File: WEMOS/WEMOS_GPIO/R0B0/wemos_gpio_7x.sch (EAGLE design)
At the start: 24 parts

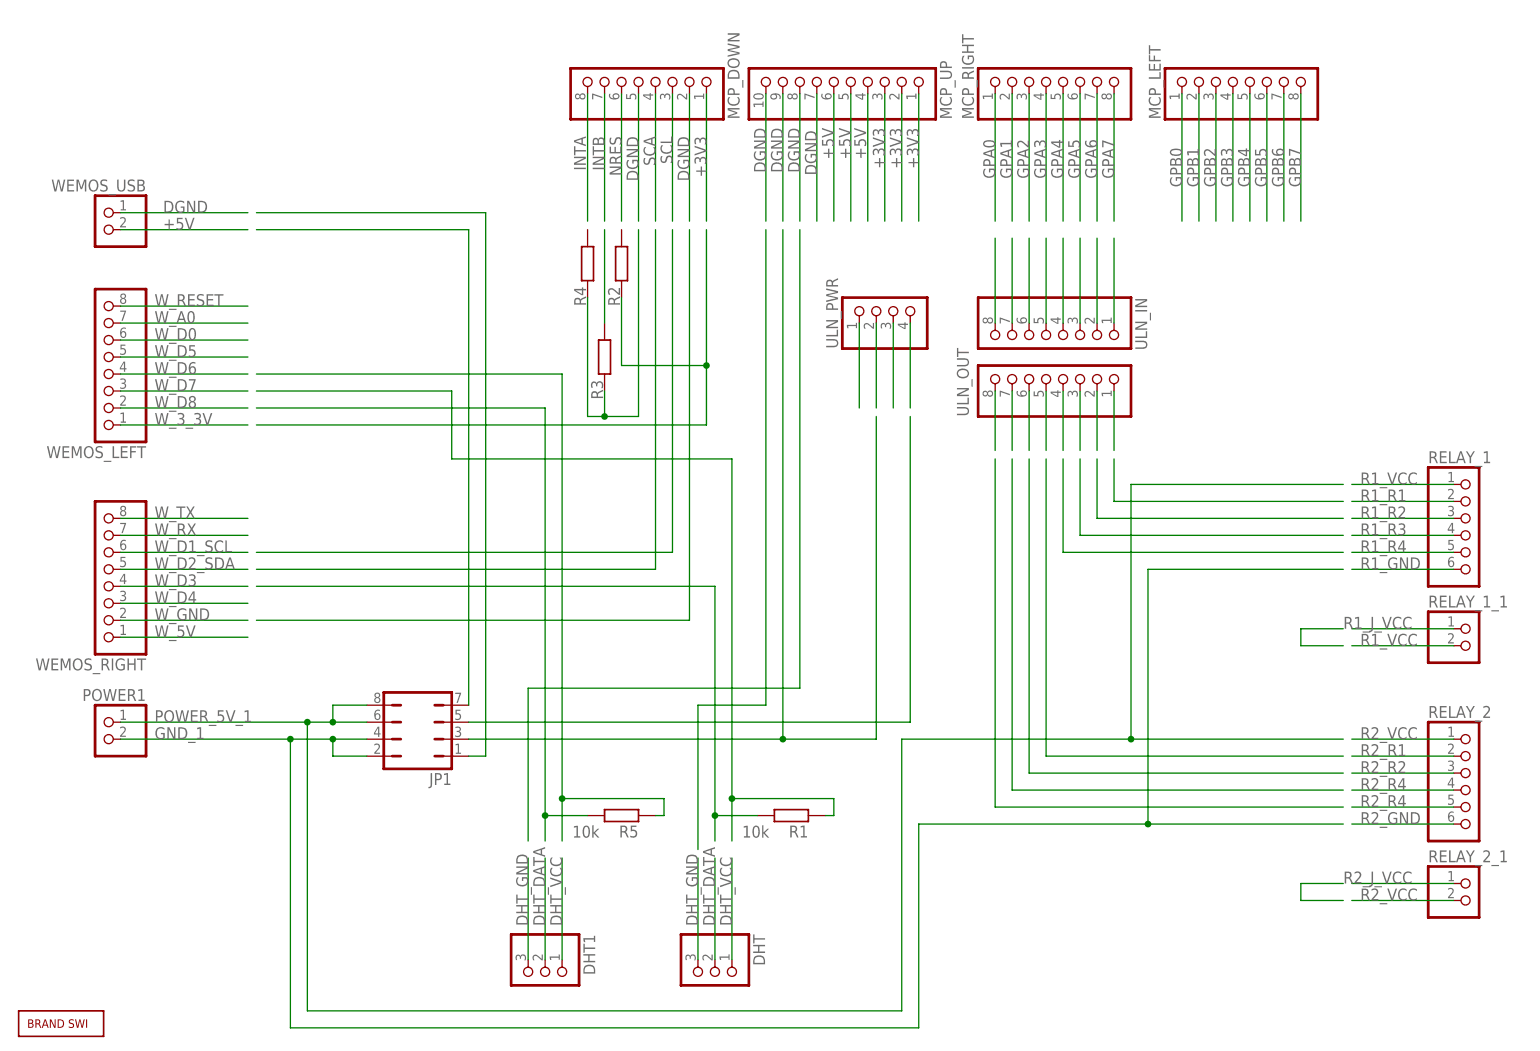
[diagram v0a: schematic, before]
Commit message: reworked wemos gpio, reworked wiring for garden control
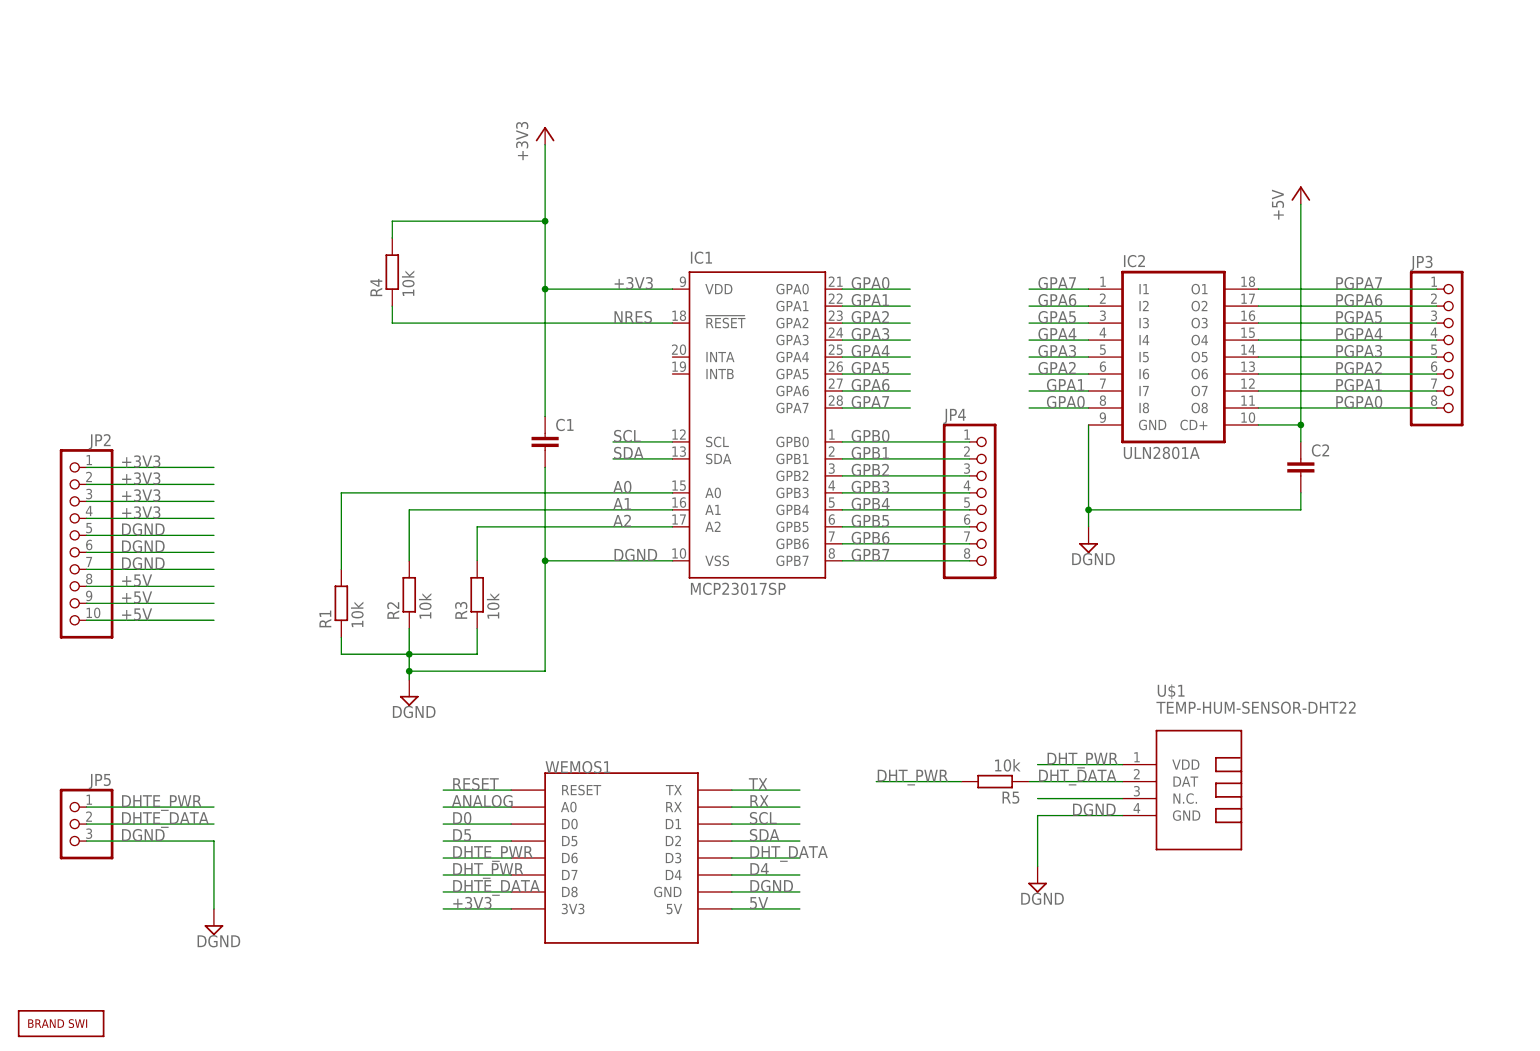
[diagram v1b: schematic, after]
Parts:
- removed DHT, DHT1: (no value), pinhead:PINHD-1X3
- removed JP1: (no value), jumper:JP4Q
- removed MCP_DOWN, MCP_LEFT, MCP_RIGHT, ULN_IN, ULN_OUT, WEMOS_LEFT, WEMOS_RIGHT: (no value), pinhead:PINHD-1X8
- removed MCP_UP: (no value), pinhead:PINHD-1X10
- removed POWER1, RELAY_1_1, RELAY_2_1, WEMOS_USB: (no value), pinhead:PINHD-1X2
- removed RELAY_1, RELAY_2: (no value), pinhead:PINHD-1X6
- removed ULN_PWR: (no value), pinhead:PINHD-1X4
- added C1, C2: (no value), rcl:C-EUC1210
- added IC1: MCP23017SP, SWI_COMMONS:MCP23017SP
- added IC2: ULN2801A, uln-udn:ULN2801A
- added JP2: (no value), pinhead:PINHD-1X10
- added JP3, JP4: (no value), pinhead:PINHD-1X8
- added JP5: (no value), pinhead:PINHD-1X3
- added U$1: TEMP-HUM-SENSOR-DHT22, SWI_COMMONS:TEMP-HUM-SENSOR-DHT22
- added WEMOS1: (no value), SWI_COMMONS:WEMOS-D1-MINI
- R1, R5: device rcl:R-EU_0207/10 -> rcl@1:R-EU_M1206
- R2, R3, R4: value (none) -> 10k; device rcl:R-EU_0204/7 -> rcl@1:R-EU_M1206
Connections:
- removed net DHT_GND: DHT.3, DHT1.3
- removed net DHT_VCC: DHT.1, DHT1.1
- removed net GND_1: JP1.2, JP1.4, POWER1.2
- removed net INTA: MCP_DOWN.8
- removed net INTB: MCP_DOWN.7
- removed net N$1: R2.1
- removed net N$11: JP1.5
- removed net N$12: JP1.1
- removed net N$13: ULN_OUT.1
- removed net N$14: ULN_OUT.2
- removed net N$15: ULN_OUT.3
- removed net N$16: ULN_OUT.4
- removed net N$17: ULN_OUT.5
- removed net N$18: ULN_OUT.6
- removed net N$19: ULN_OUT.7
- removed net N$20: ULN_OUT.8
- removed net N$21: R5.2
- removed net N$23: ULN_IN.1
- removed net N$24: ULN_IN.2
- removed net N$25: ULN_IN.3
- removed net N$26: ULN_IN.4
- removed net N$27: ULN_IN.5
- removed net N$28: ULN_IN.6
- removed net N$29: ULN_IN.7
- removed net N$30: ULN_IN.8
- removed net N$31: R5.1
- removed net N$32: R3.1, R4.1
- removed net N$33: R3.2
- removed net N$4: R1.2
- removed net N$49: ULN_PWR.1
- removed net N$5: R1.1
- removed net N$50: ULN_PWR.2
- removed net N$51: ULN_PWR.3
- removed net N$52: ULN_PWR.4
- removed net N$8: JP1.7
- removed net N$9: JP1.3
- removed net POWER_5V_1: JP1.6, JP1.8, POWER1.1
- removed net R1_GND: RELAY_1.6
- removed net R1_J_VCC: RELAY_1_1.1
- removed net R1_R1: RELAY_1.2
- removed net R1_R2: RELAY_1.3
- removed net R1_R3: RELAY_1.4
- removed net R1_R4: RELAY_1.5
- removed net R1_VCC: RELAY_1.1, RELAY_1_1.2
- removed net R2_GND: RELAY_2.6
- removed net R2_J_VCC: RELAY_2_1.1
- removed net R2_R1: RELAY_2.2
- removed net R2_R2: RELAY_2.3
- removed net R2_R4: RELAY_2.4, RELAY_2.5
- removed net R2_VCC: RELAY_2.1, RELAY_2_1.2
- removed net SCA: MCP_DOWN.4
- removed net W_3_3V: WEMOS_LEFT.1
- removed net W_5V: WEMOS_RIGHT.1
- removed net W_A0: WEMOS_LEFT.7
- removed net W_D0: WEMOS_LEFT.6
- removed net W_D1_SCL: WEMOS_RIGHT.6
- removed net W_D2_SDA: WEMOS_RIGHT.5
- removed net W_D3: WEMOS_RIGHT.4
- removed net W_D4: WEMOS_RIGHT.3
- removed net W_D5: WEMOS_LEFT.5
- removed net W_D6: WEMOS_LEFT.4
- removed net W_D7: WEMOS_LEFT.3
- removed net W_D8: WEMOS_LEFT.2
- removed net W_GND: WEMOS_RIGHT.2
- removed net W_RESET: WEMOS_LEFT.8
- removed net W_RX: WEMOS_RIGHT.7
- removed net W_TX: WEMOS_RIGHT.8
- new net 5V: WEMOS1.5V
- new net A0: IC1.A0, R1.2
- new net A1: IC1.A1, R2.2
- new net A2: IC1.A2, R3.2
- new net ANALOG: WEMOS1.A0
- new net D0: WEMOS1.D0
- new net D4: WEMOS1.D4
- new net D5: WEMOS1.D5
- new net DHTE_DATA: JP5.2, WEMOS1.D8
- new net DHTE_PWR: JP5.1, WEMOS1.D6
- new net DHT_PWR: R5.2, U$1.VDD, WEMOS1.D7
- new net N$3: U$1.N.C.
- new net PGPA0: IC2.O8, JP3.8
- new net PGPA1: IC2.O7, JP3.7
- new net PGPA2: IC2.O6, JP3.6
- new net PGPA3: IC2.O5, JP3.5
- new net PGPA4: IC2.O4, JP3.4
- new net PGPA5: IC2.O3, JP3.3
- new net PGPA6: IC2.O2, JP3.2
- new net PGPA7: IC2.O1, JP3.1
- new net RESET: WEMOS1.RESET
- new net RX: WEMOS1.RX
- new net SDA: IC1.SDA, WEMOS1.D2
- net +3V3: now also C1.1, IC1.VDD, JP2.1, JP2.2, JP2.3, JP2.4, R4.2, WEMOS1.3V3; no longer MCP_DOWN.1, MCP_UP.1, MCP_UP.2, MCP_UP.3
- net +5V: now also C2.1, IC2.CD+, JP2.10, JP2.8, JP2.9; no longer MCP_UP.5, MCP_UP.6, WEMOS_USB.2
- net DGND: now also C1.2, C2.2, IC1.VSS, IC2.GND, JP2.5, JP2.6, JP2.7, JP5.3, R1.1, R2.1, R3.1, U$1.GND, WEMOS1.GND; no longer MCP_DOWN.2, MCP_DOWN.5, MCP_UP.10, MCP_UP.8, MCP_UP.9, WEMOS_USB.1
- net DHT_DATA: now also R5.1, U$1.DAT, WEMOS1.D3; no longer DHT.2, DHT1.2
- net GPA0: now also IC1.GPA0, IC2.I8; no longer MCP_RIGHT.1
- net GPA1: now also IC1.GPA1, IC2.I7; no longer MCP_RIGHT.2
- net GPA2: now also IC1.GPA2, IC2.I6; no longer MCP_RIGHT.3
- net GPA3: now also IC1.GPA3, IC2.I5; no longer MCP_RIGHT.4
- net GPA4: now also IC1.GPA4, IC2.I4; no longer MCP_RIGHT.5
- net GPA5: now also IC1.GPA5, IC2.I3; no longer MCP_RIGHT.6
- net GPA6: now also IC1.GPA6, IC2.I2; no longer MCP_RIGHT.7
- net GPA7: now also IC1.GPA7, IC2.I1; no longer MCP_RIGHT.8
- net GPB0: now also IC1.GPB0, JP4.1; no longer MCP_LEFT.1
- net GPB1: now also IC1.GPB1, JP4.2; no longer MCP_LEFT.2
- net GPB2: now also IC1.GPB2, JP4.3; no longer MCP_LEFT.3
- net GPB3: now also IC1.GPB3, JP4.4; no longer MCP_LEFT.4
- net GPB4: now also IC1.GPB4, JP4.5; no longer MCP_LEFT.5
- net GPB5: now also IC1.GPB5, JP4.6; no longer MCP_LEFT.6
- net GPB6: now also IC1.GPB6, JP4.7; no longer MCP_LEFT.7
- net GPB7: now also IC1.GPB7, JP4.8; no longer MCP_LEFT.8
- net NRES: now also IC1.!RESET, R4.1; no longer MCP_DOWN.6
- net SCL: now also IC1.SCL, WEMOS1.D1; no longer MCP_DOWN.3
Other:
- moved on the sheet: R1, R2, R3, R4, R5
